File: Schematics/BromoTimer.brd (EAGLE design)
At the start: 101.6 x 80 mm, 29 parts, among them IC1 PIC16F687, IC2 7805TV, K1 G2R2A, K2 G2R2A, Q1 BC548B, Q2 BC548B, Q3 BC548B, X1 AC_IN, X4 22-23-2041, X5 AC_OUT

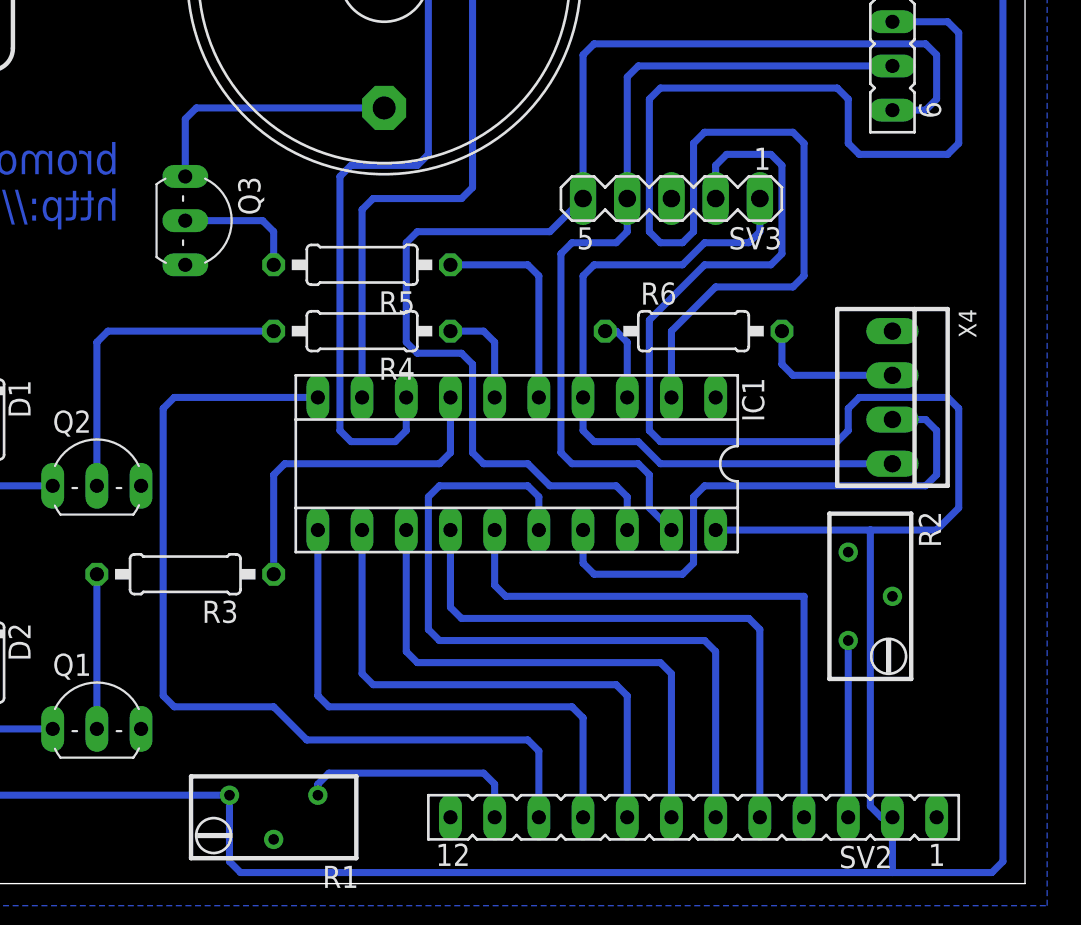
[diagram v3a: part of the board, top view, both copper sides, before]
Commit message: moved R2, R4, R5 and Q3 to better positions.
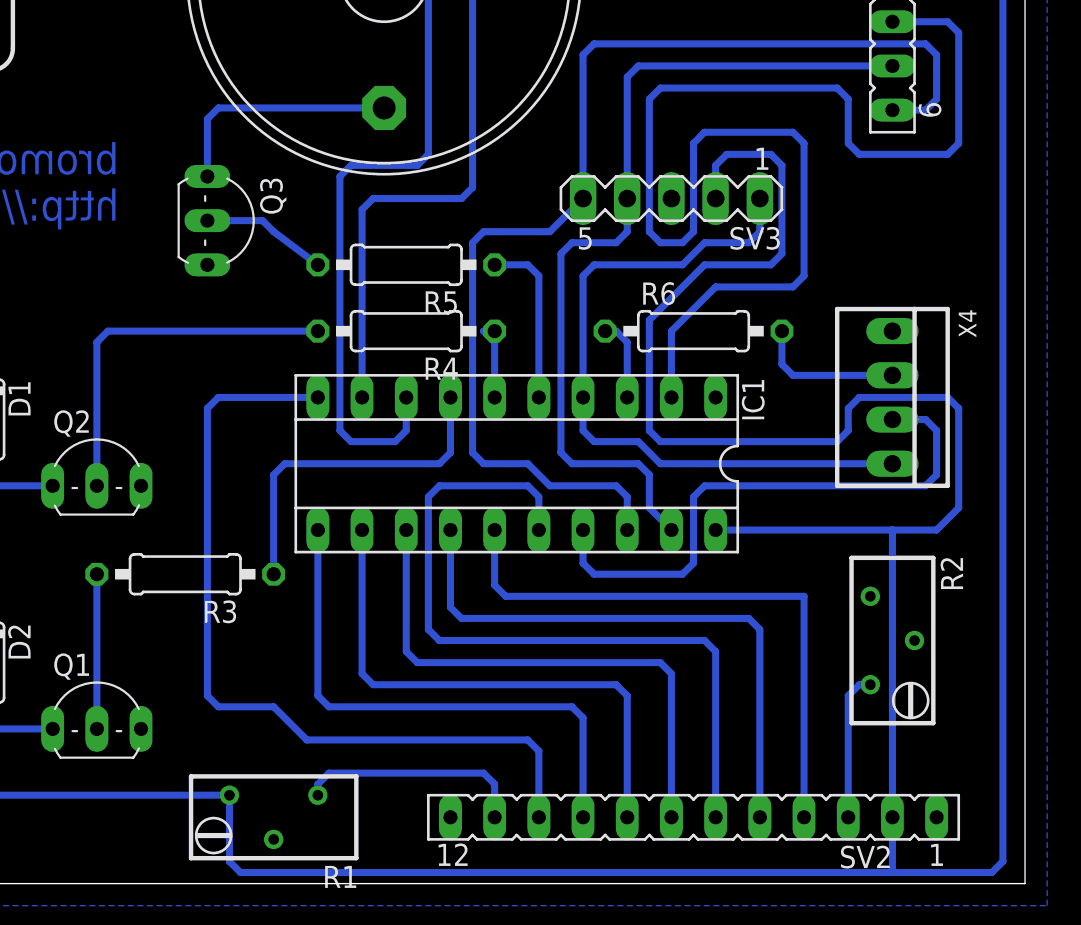
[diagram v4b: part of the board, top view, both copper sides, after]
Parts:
- moved R2 2.84 mm to (94.0, 14.0)
- moved R4 2.54 mm to (66.0, 31.8)
- moved R5 2.54 mm to (66.0, 35.6)
- moved Q3 1.27 mm to (55.9, 38.1)
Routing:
- net B: track 72.6 -> 65.8 mm
- net B3: track 52.4 -> 47.3 mm
- net N$17: track 12.3 -> 9.79 mm
- net N$4: track 18.7 -> 21.2 mm
- net N$3: track 10.2 -> 8.52 mm
- net N$19: track 15.0 -> 13.7 mm
- net N$14: track 5.98 -> 4.71 mm
- net +5V: track 286.4 -> 285.5 mm
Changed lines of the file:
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@@
 <element name="C2" library="rcl" package="C025-024X044" value="100n" x="88.9" y="63.5" rot="R180"/>
 <element name="R1" library="rcl" package="RTRIMT93YB" value="100k" x="58.42" y="3.81" rot="R90"/>
-<element name="R2" library="rcl" package="RTRIMT93YB" value="100k" x="92.71" y="16.51" rot="R180"/>
+<element name="R2" library="rcl" package="RTRIMT93YB" value="100k" x="93.98" y="13.97" rot="R180"/>
 <element name="Q1" library="transistor-npn" package="TO92-EBC" value="BC548B" x="48.26" y="10.16"/>
 <element name="Q2" library="transistor-npn" package="TO92-EBC" value="BC548B" x="48.26" y="24.13"/>
 <element name="R3" library="rcl" package="0207/10" value="" x="53.34" y="17.78" rot="R180"/>
-<element name="R4" library="rcl" package="0207/10" value="" x="63.5" y="31.75" rot="R180"/>
+<element name="R4" library="rcl" package="0207/10" value="" x="66.04" y="31.75" rot="R180"/>
 <element name="K1" library="relay" package="G2R2A" value="G2R2A" x="34.29" y="12.7" rot="R180">
 <attribute name="OC_NEWARK" value="36M5257" x="-6.35" y="66.04" size="1.778" layer="27" rot="R180" display="off"/>
@@
 </element>
 <element name="D3" library="diode" package="DO41-10" value="1N4004" x="96.52" y="71.12" rot="R270"/>
-<element name="Q3" library="transistor-npn" package="TO92-EBC" value="BC548B" x="54.61" y="38.1" rot="R270"/>
-<element name="R5" library="rcl" package="0207/10" value="" x="63.5" y="35.56" rot="R180"/>
+<element name="Q3" library="transistor-npn" package="TO92-EBC" value="BC548B" x="55.88" y="38.1" rot="R270"/>
+<element name="R5" library="rcl" package="0207/10" value="" x="66.04" y="35.56" rot="R180"/>
 <element name="X4" library="con-molex" package="22-23-2041" value="22-23-2041" x="93.98" y="27.94" rot="R270">
 <attribute name="OC_NEWARK" value="38C0355" x="27.94" y="-34.29" size="1.778" layer="27" rot="R270" display="off"/>
@@
 <wire x1="100.33" y1="62.865" x2="99.695" y2="63.5" width="0.4064" layer="16"/>
 <wire x1="99.695" y1="63.5" x2="90.17" y2="63.5" width="0.4064" layer="16"/>
-<wire x1="83.82" y1="20.32" x2="92.71" y2="20.32" width="0.4064" layer="16"/>
+<wire x1="83.82" y1="20.32" x2="93.98" y2="20.32" width="0.4064" layer="16"/>
 <wire x1="36.83" y1="30.353" x2="34.925" y2="30.353" width="0.4064" layer="16"/>
 <wire x1="34.925" y1="30.353" x2="34.29" y2="29.718" width="0.4064" layer="16"/>
@@
 <wire x1="90.805" y1="25.4" x2="91.44" y2="26.035" width="0.4064" layer="16"/>
 <wire x1="91.44" y1="26.035" x2="91.44" y2="27.305" width="0.4064" layer="16"/>
-<wire x1="92.71" y1="20.32" x2="92.71" y2="4.445" width="0.4064" layer="16"/>
-<wire x1="92.71" y1="4.445" x2="93.345" y2="3.81" width="0.4064" layer="16"/>
-<wire x1="93.345" y1="3.81" x2="93.98" y2="3.81" width="0.4064" layer="16"/>
+<wire x1="93.98" y1="20.32" x2="93.98" y2="3.81" width="0.4064" layer="16"/>
 <wire x1="91.44" y1="27.305" x2="92.075" y2="27.94" width="0.4064" layer="16"/>
 <wire x1="92.075" y1="27.94" x2="97.155" y2="27.94" width="0.4064" layer="16"/>
@@
 <wire x1="97.79" y1="27.305" x2="97.79" y2="21.59" width="0.4064" layer="16"/>
 <wire x1="97.79" y1="21.59" x2="96.52" y2="20.32" width="0.4064" layer="16"/>
-<wire x1="96.52" y1="20.32" x2="92.71" y2="20.32" width="0.4064" layer="16"/>
+<wire x1="96.52" y1="20.32" x2="93.98" y2="20.32" width="0.4064" layer="16"/>
 <wire x1="55.88" y1="5.08" x2="34.925" y2="5.08" width="0.4064" layer="16"/>
 <wire x1="34.925" y1="5.08" x2="34.29" y2="5.715" width="0.4064" layer="16"/>
@@
 <wire x1="73.025" y1="8.255" x2="60.325" y2="8.255" width="0.4064" layer="16"/>
 <wire x1="60.325" y1="8.255" x2="58.42" y2="10.16" width="0.4064" layer="16"/>
-<wire x1="58.42" y1="10.16" x2="52.705" y2="10.16" width="0.4064" layer="16"/>
-<wire x1="52.705" y1="10.16" x2="52.07" y2="10.795" width="0.4064" layer="16"/>
-<wire x1="52.07" y1="10.795" x2="52.07" y2="27.305" width="0.4064" layer="16"/>
-<wire x1="52.07" y1="27.305" x2="52.705" y2="27.94" width="0.4064" layer="16"/>
-<wire x1="52.705" y1="27.94" x2="60.96" y2="27.94" width="0.4064" layer="16"/>
+<wire x1="58.42" y1="10.16" x2="55.245" y2="10.16" width="0.4064" layer="16"/>
+<wire x1="55.245" y1="10.16" x2="54.61" y2="10.795" width="0.4064" layer="16"/>
+<wire x1="54.61" y1="10.795" x2="54.61" y2="27.305" width="0.4064" layer="16"/>
+<wire x1="54.61" y1="27.305" x2="55.245" y2="27.94" width="0.4064" layer="16"/>
+<wire x1="55.245" y1="27.94" x2="60.96" y2="27.94" width="0.4064" layer="16"/>
 </signal>
 <signal name="N$1">
@@
 <contactref element="SV2" pad="3"/>
 <contactref element="R2" pad="3"/>
-<wire x1="91.44" y1="3.81" x2="91.44" y2="13.97" width="0.4064" layer="16"/>
+<wire x1="91.44" y1="3.81" x2="91.44" y2="10.795" width="0.4064" layer="16"/>
+<wire x1="91.44" y1="10.795" x2="92.075" y2="11.43" width="0.4064" layer="16"/>
+<wire x1="92.075" y1="11.43" x2="92.71" y2="11.43" width="0.4064" layer="16"/>
 </signal>
 <signal name="L1">
@@
 <contactref element="SV3" pad="5"/>
 <wire x1="70.485" y1="24.13" x2="69.85" y2="24.765" width="0.4064" layer="16"/>
-<wire x1="69.85" y1="24.765" x2="69.85" y2="29.845" width="0.4064" layer="16"/>
-<wire x1="69.85" y1="29.845" x2="69.215" y2="30.48" width="0.4064" layer="16"/>
-<wire x1="69.215" y1="30.48" x2="66.675" y2="30.48" width="0.4064" layer="16"/>
-<wire x1="66.675" y1="30.48" x2="66.04" y2="31.115" width="0.4064" layer="16"/>
-<wire x1="66.04" y1="31.115" x2="66.04" y2="36.83" width="0.4064" layer="16"/>
-<wire x1="66.04" y1="36.83" x2="66.675" y2="37.465" width="0.4064" layer="16"/>
-<wire x1="66.675" y1="37.465" x2="74.295" y2="37.465" width="0.4064" layer="16"/>
+<wire x1="69.85" y1="24.765" x2="69.85" y2="36.83" width="0.4064" layer="16"/>
+<wire x1="69.85" y1="36.83" x2="70.485" y2="37.465" width="0.4064" layer="16"/>
+<wire x1="70.485" y1="37.465" x2="74.295" y2="37.465" width="0.4064" layer="16"/>
 <wire x1="74.295" y1="37.465" x2="76.2" y2="39.37" width="0.4064" layer="16"/>
 <wire x1="76.2" y1="39.37" x2="76.2" y2="47.625" width="0.4064" layer="16"/>
@@
 <contactref element="R4" pad="2"/>
 <contactref element="Q2" pad="B"/>
-<wire x1="58.42" y1="31.75" x2="48.895" y2="31.75" width="0.4064" layer="16"/>
+<wire x1="60.96" y1="31.75" x2="48.895" y2="31.75" width="0.4064" layer="16"/>
 <wire x1="48.895" y1="31.75" x2="48.26" y2="31.115" width="0.4064" layer="16"/>
 <wire x1="48.26" y1="31.115" x2="48.26" y2="22.86" width="0.4064" layer="16"/>
@@
 <contactref element="IC1" pad="6"/>
 <contactref element="R4" pad="1"/>
-<wire x1="68.58" y1="31.75" x2="70.485" y2="31.75" width="0.4064" layer="16"/>
+<wire x1="71.12" y1="31.75" x2="70.485" y2="31.75" width="0.4064" layer="16"/>
 <wire x1="70.485" y1="31.75" x2="71.12" y2="31.115" width="0.4064" layer="16"/>
 <wire x1="71.12" y1="31.115" x2="71.12" y2="27.94" width="0.4064" layer="16"/>
@@
 <wire x1="73.66" y1="27.94" x2="73.66" y2="34.925" width="0.4064" layer="16"/>
 <wire x1="73.66" y1="34.925" x2="73.025" y2="35.56" width="0.4064" layer="16"/>
-<wire x1="73.025" y1="35.56" x2="68.58" y2="35.56" width="0.4064" layer="16"/>
+<wire x1="73.025" y1="35.56" x2="71.12" y2="35.56" width="0.4064" layer="16"/>
 </signal>
 <signal name="N$18">
 <contactref element="Q3" pad="B"/>
 <contactref element="R5" pad="2"/>
-<wire x1="53.34" y1="38.1" x2="57.785" y2="38.1" width="0.4064" layer="16"/>
+<wire x1="54.61" y1="38.1" x2="57.785" y2="38.1" width="0.4064" layer="16"/>
 <wire x1="57.785" y1="38.1" x2="58.42" y2="37.465" width="0.4064" layer="16"/>
-<wire x1="58.42" y1="37.465" x2="58.42" y2="35.56" width="0.4064" layer="16"/>
+<wire x1="58.42" y1="37.465" x2="60.96" y2="35.56" width="0.4064" layer="16"/>
 </signal>
 <signal name="N$19">
 <contactref element="Q3" pad="C"/>
 <contactref element="SG1" pad="-"/>
-<wire x1="53.34" y1="40.64" x2="53.34" y2="43.942" width="0.4064" layer="16"/>
-<wire x1="53.34" y1="43.942" x2="53.975" y2="44.577" width="0.4064" layer="16"/>
-<wire x1="53.975" y1="44.577" x2="64.77" y2="44.577" width="0.4064" layer="16"/>
+<wire x1="54.61" y1="40.64" x2="54.61" y2="43.942" width="0.4064" layer="16"/>
+<wire x1="54.61" y1="43.942" x2="55.245" y2="44.577" width="0.4064" layer="16"/>
+<wire x1="55.245" y1="44.577" x2="64.77" y2="44.577" width="0.4064" layer="16"/>
 </signal>
 <signal name="N$20">

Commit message: Clean up R1
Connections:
- net +5V: now also R1.2; no longer R1.3
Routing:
- net +5V: track 285.5 -> 287.8 mm
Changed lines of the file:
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@@
 <layer number="18" name="Vias" color="2" fill="1" visible="yes" active="yes"/>
 <layer number="19" name="Unrouted" color="6" fill="1" visible="yes" active="yes"/>
-<layer number="20" name="Dimension" color="15" fill="1" visible="yes" active="yes"/>
-<layer number="21" name="tPlace" color="7" fill="1" visible="yes" active="yes"/>
-<layer number="22" name="bPlace" color="7" fill="1" visible="yes" active="yes"/>
-<layer number="23" name="tOrigins" color="15" fill="1" visible="yes" active="yes"/>
-<layer number="24" name="bOrigins" color="15" fill="1" visible="yes" active="yes"/>
-<layer number="25" name="tNames" color="7" fill="1" visible="yes" active="yes"/>
-<layer number="26" name="bNames" color="7" fill="1" visible="yes" active="yes"/>
-<layer number="27" name="tValues" color="7" fill="1" visible="yes" active="yes"/>
-<layer number="28" name="bValues" color="7" fill="1" visible="yes" active="yes"/>
+<layer number="20" name="Dimension" color="15" fill="1" visible="no" active="yes"/>
+<layer number="21" name="tPlace" color="7" fill="1" visible="no" active="yes"/>
+<layer number="22" name="bPlace" color="7" fill="1" visible="no" active="yes"/>
+<layer number="23" name="tOrigins" color="15" fill="1" visible="no" active="yes"/>
+<layer number="24" name="bOrigins" color="15" fill="1" visible="no" active="yes"/>
+<layer number="25" name="tNames" color="7" fill="1" visible="no" active="yes"/>
+<layer number="26" name="bNames" color="7" fill="1" visible="no" active="yes"/>
+<layer number="27" name="tValues" color="7" fill="1" visible="no" active="yes"/>
+<layer number="28" name="bValues" color="7" fill="1" visible="no" active="yes"/>
 <layer number="29" name="tStop" color="7" fill="3" visible="no" active="yes"/>
 <layer number="30" name="bStop" color="7" fill="6" visible="no" active="yes"/>
@@
 <layer number="37" name="tTest" color="7" fill="1" visible="no" active="yes"/>
 <layer number="38" name="bTest" color="7" fill="1" visible="no" active="yes"/>
-<layer number="39" name="tKeepout" color="4" fill="11" visible="yes" active="yes"/>
-<layer number="40" name="bKeepout" color="1" fill="11" visible="yes" active="yes"/>
-<layer number="41" name="tRestrict" color="4" fill="10" visible="yes" active="yes"/>
-<layer number="42" name="bRestrict" color="1" fill="10" visible="yes" active="yes"/>
-<layer number="43" name="vRestrict" color="2" fill="10" visible="yes" active="yes"/>
+<layer number="39" name="tKeepout" color="4" fill="11" visible="no" active="yes"/>
+<layer number="40" name="bKeepout" color="1" fill="11" visible="no" active="yes"/>
+<layer number="41" name="tRestrict" color="4" fill="10" visible="no" active="yes"/>
+<layer number="42" name="bRestrict" color="1" fill="10" visible="no" active="yes"/>
+<layer number="43" name="vRestrict" color="2" fill="10" visible="no" active="yes"/>
 <layer number="44" name="Drills" color="7" fill="1" visible="no" active="yes"/>
 <layer number="45" name="Holes" color="7" fill="1" visible="no" active="yes"/>
 <layer number="46" name="Milling" color="3" fill="1" visible="no" active="yes"/>
 <layer number="47" name="Measures" color="7" fill="1" visible="no" active="yes"/>
-<layer number="48" name="Document" color="7" fill="1" visible="yes" active="yes"/>
-<layer number="49" name="Reference" color="7" fill="1" visible="yes" active="yes"/>
+<layer number="48" name="Document" color="7" fill="1" visible="no" active="yes"/>
+<layer number="49" name="Reference" color="7" fill="1" visible="no" active="yes"/>
 <layer number="50" name="dxf" color="7" fill="1" visible="no" active="no"/>
-<layer number="51" name="tDocu" color="7" fill="1" visible="yes" active="yes"/>
-<layer number="52" name="bDocu" color="7" fill="1" visible="yes" active="yes"/>
+<layer number="51" name="tDocu" color="7" fill="1" visible="no" active="yes"/>
+<layer number="52" name="bDocu" color="7" fill="1" visible="no" active="yes"/>
 <layer number="53" name="tGND_GNDA" color="7" fill="9" visible="no" active="no"/>
 <layer number="54" name="bGND_GNDA" color="1" fill="9" visible="no" active="no"/>
@@
 <contactref element="IC1" pad="20"/>
 <contactref element="SV2" pad="2"/>
-<contactref element="R1" pad="3"/>
 <contactref element="SV3" pad="2"/>
 <contactref element="IC2" pad="3"/>
@@
 <wire x1="95.885" y1="69.85" x2="90.17" y2="69.85" width="0.4064" layer="16"/>
 <wire x1="90.17" y1="63.5" x2="90.17" y2="69.85" width="0.4064" layer="16"/>
-<wire x1="55.88" y1="5.08" x2="55.88" y2="1.27" width="0.4064" layer="16"/>
-<wire x1="55.88" y1="1.27" x2="56.515" y2="0.635" width="0.4064" layer="16"/>
-<wire x1="56.515" y1="0.635" x2="93.98" y2="0.635" width="0.4064" layer="16"/>
+<wire x1="34.29" y1="1.27" x2="34.925" y2="0.635" width="0.4064" layer="16"/>
+<wire x1="34.925" y1="0.635" x2="58.42" y2="0.635" width="0.4064" layer="16"/>
+<wire x1="58.42" y1="0.635" x2="93.98" y2="0.635" width="0.4064" layer="16"/>
 <wire x1="93.98" y1="3.81" x2="93.98" y2="0.635" width="0.4064" layer="16"/>
 <wire x1="93.98" y1="0.635" x2="99.695" y2="0.635" width="0.4064" layer="16"/>
@@
 <wire x1="97.79" y1="21.59" x2="96.52" y2="20.32" width="0.4064" layer="16"/>
 <wire x1="96.52" y1="20.32" x2="93.98" y2="20.32" width="0.4064" layer="16"/>
-<wire x1="55.88" y1="5.08" x2="34.925" y2="5.08" width="0.4064" layer="16"/>
-<wire x1="34.925" y1="5.08" x2="34.29" y2="5.715" width="0.4064" layer="16"/>
-<wire x1="34.29" y1="5.715" x2="34.29" y2="16.51" width="0.4064" layer="16"/>
+<wire x1="34.29" y1="1.27" x2="34.29" y2="16.51" width="0.4064" layer="16"/>
+<contactref element="R1" pad="2"/>
+<wire x1="58.42" y1="2.54" x2="58.42" y2="0.635" width="0.4064" layer="16"/>
 </signal>
 <signal name="GND">
